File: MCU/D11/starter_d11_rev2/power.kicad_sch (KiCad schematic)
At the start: 8 parts, among them J4 out_5V0, J5 out_3V3, U3 TLV73333/SOT-23

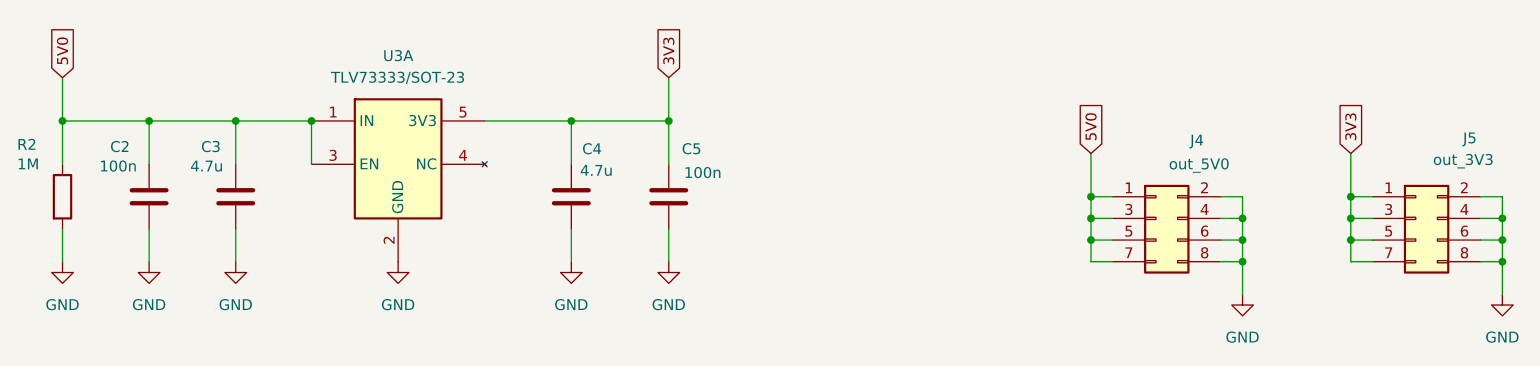
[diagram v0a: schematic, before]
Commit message: D11 schematics and PCB updates - printed prototype version
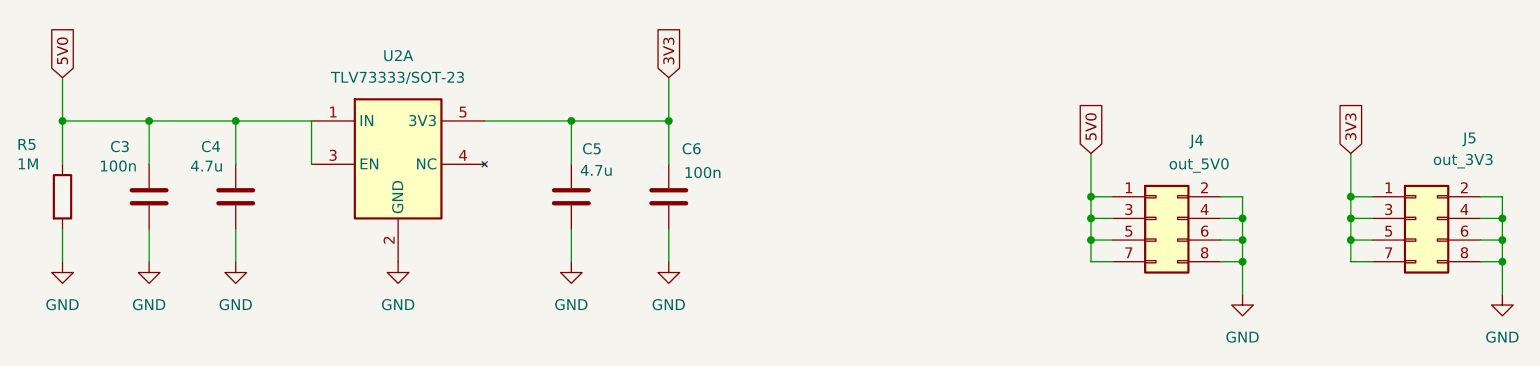
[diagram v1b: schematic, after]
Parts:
- renumbered C2 to C3, C3 to C4, C4 to C5, C5 to C6, R2 to R5, U3 to U2
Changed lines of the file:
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@@
-	)
-	(junction
-		(at 95.25 66.04)
-		(diameter 0)
-		(color 0 0 0 0)
 	)
 	(junction
@@
 		(on_board yes)
 		(dnp no)
-		(property "Reference" "C5"
+		(property "Reference" "C6"
 			(at 138.684 69.342 0)
 			(effects
@@
 			(project "starter_d11_rev2"
 				(path "/2c4ac472-9624-49c1-b7f6-74967546e3f5/b4cd3d0d-2c28-4d1a-b5ce-b0f6d285c299"
-					(reference "C5")
+					(reference "C6")
 					(unit 1)
 				)
@@
 		(on_board yes)
 		(dnp no)
-		(property "Reference" "C2"
+		(property "Reference" "C3"
 			(at 71.628 69.088 0)
 			(effects
@@
 			(project "starter_d11_rev2"
 				(path "/2c4ac472-9624-49c1-b7f6-74967546e3f5/b4cd3d0d-2c28-4d1a-b5ce-b0f6d285c299"
-					(reference "C2")
+					(reference "C3")
 					(unit 1)
 				)
@@
 		(on_board yes)
 		(dnp no)
-		(property "Reference" "C3"
+		(property "Reference" "C4"
 			(at 82.296 69.088 0)
 			(effects
@@
 			(project "starter_d11_rev2"
 				(path "/2c4ac472-9624-49c1-b7f6-74967546e3f5/b4cd3d0d-2c28-4d1a-b5ce-b0f6d285c299"
-					(reference "C3")
+					(reference "C4")
 					(unit 1)
 				)
@@
 		(dnp no)
 		(fields_autoplaced yes)
-		(property "Reference" "U3"
+		(property "Reference" "U2"
 			(at 105.41 58.42 0)
 			(effects
@@
 			(project "starter_d11_rev2"
 				(path "/2c4ac472-9624-49c1-b7f6-74967546e3f5/b4cd3d0d-2c28-4d1a-b5ce-b0f6d285c299"
-					(reference "U3")
+					(reference "U2")
 					(unit 1)
 				)
@@
 		(on_board yes)
 		(dnp no)
-		(property "Reference" "R2"
+		(property "Reference" "R5"
 			(at 60.706 68.834 0)
 			(effects
@@
 			(project "starter_d11_rev2"
 				(path "/2c4ac472-9624-49c1-b7f6-74967546e3f5/b4cd3d0d-2c28-4d1a-b5ce-b0f6d285c299"
-					(reference "R2")
+					(reference "R5")
 					(unit 1)
 				)
@@
 		(on_board yes)
 		(dnp no)
-		(property "Reference" "C4"
+		(property "Reference" "C5"
 			(at 127 69.342 0)
 			(effects
@@
 			(project "starter_d11_rev2"
 				(path "/2c4ac472-9624-49c1-b7f6-74967546e3f5/b4cd3d0d-2c28-4d1a-b5ce-b0f6d285c299"
-					(reference "C4")
+					(reference "C5")
 					(unit 1)
 				)
